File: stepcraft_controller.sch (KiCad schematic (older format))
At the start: 67 parts, among them J1 USB, J2 X1, J3 ISP, J4 Probe, J5 Spindle, J6 Serial, SW1 RST, U1 ADuM1201BR, U2 ATMEGA328P-AU, U3 CP2102, U4 ADuM1201BR, Y1 Crystal

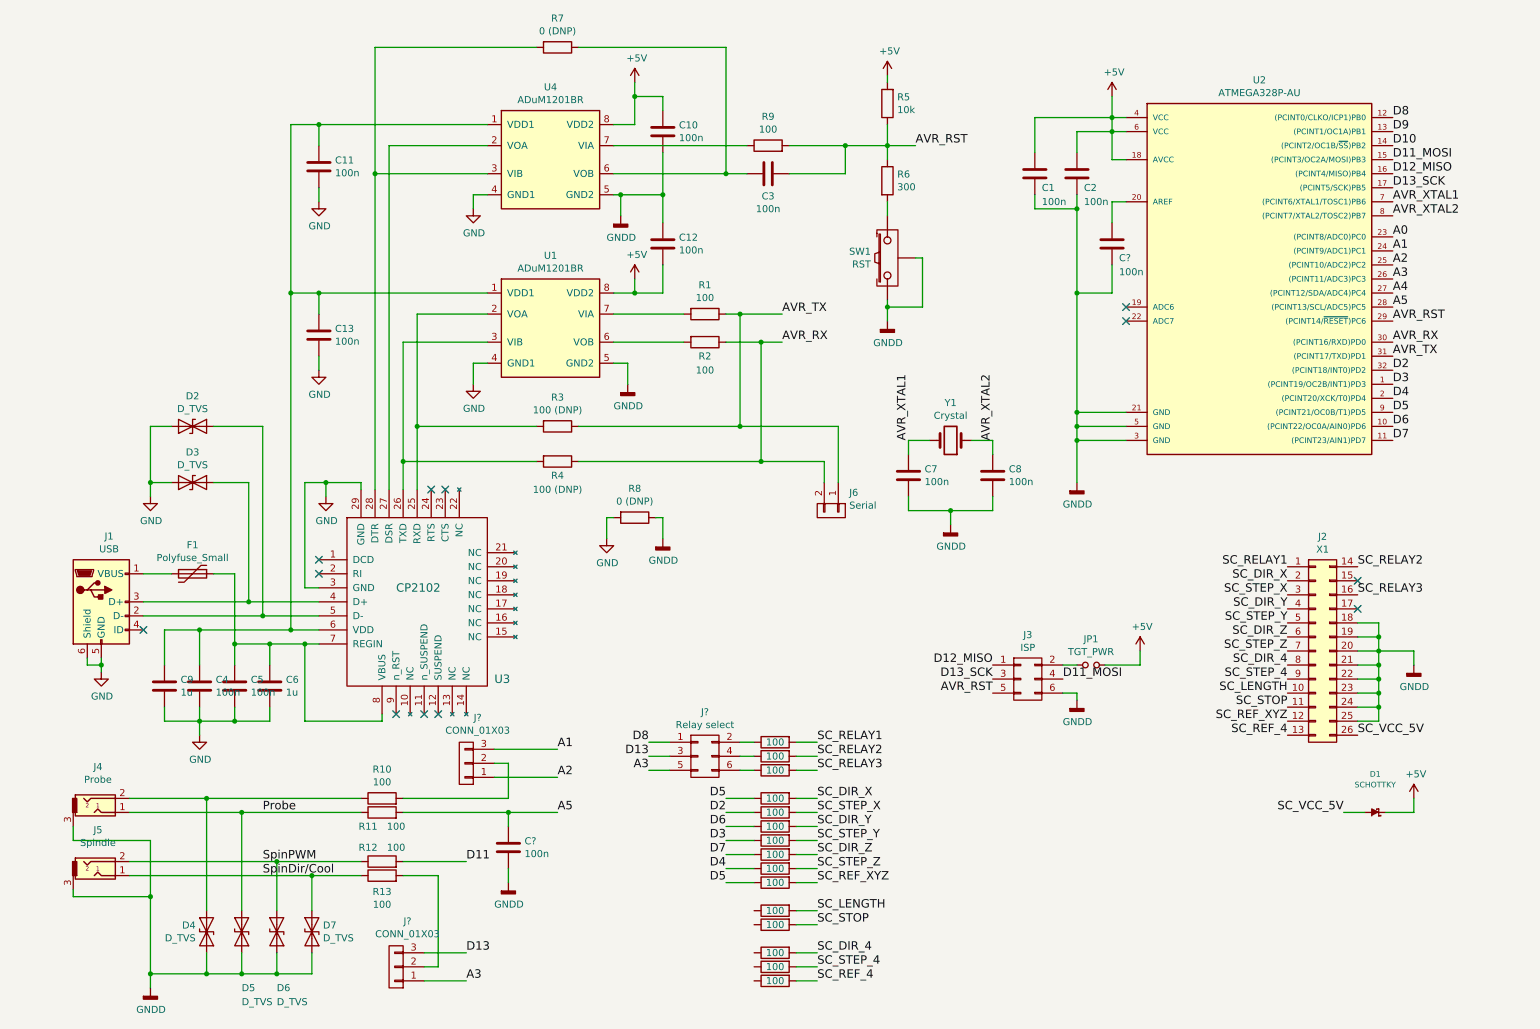
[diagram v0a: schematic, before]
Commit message: Update schematics and board, fully routed board
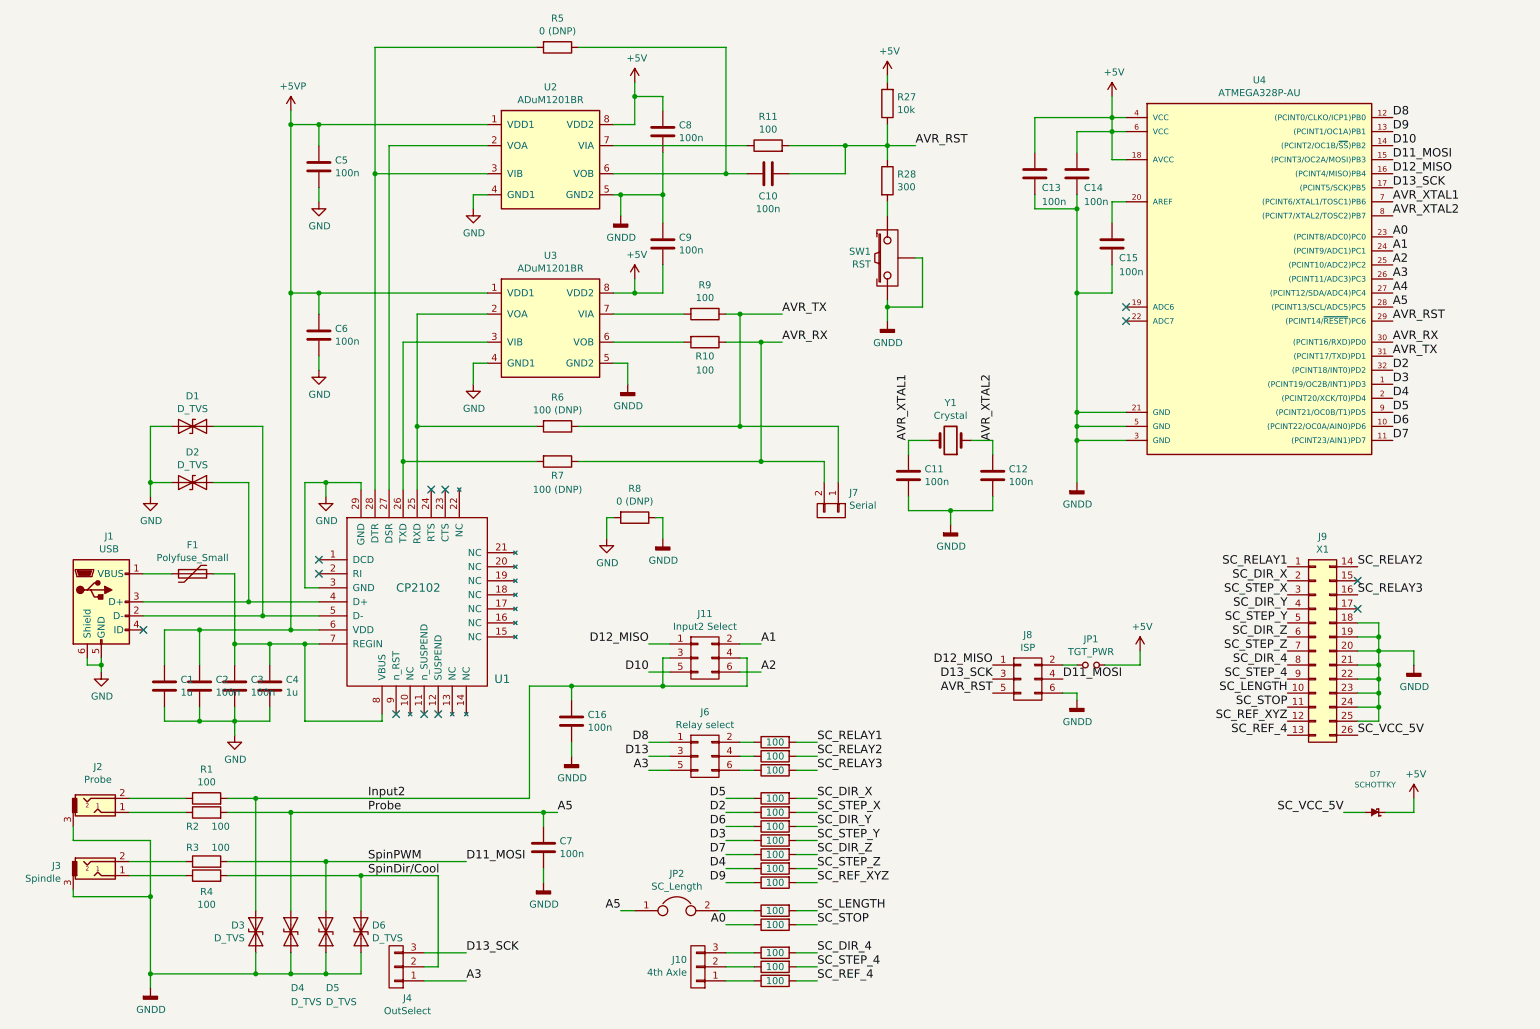
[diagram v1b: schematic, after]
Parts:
- removed J?: CONN_01X03, symbol CONN_01X03
- added C16: 100n, Capacitors_SMD:C_0805, symbol C
- added J10: 4th Axle, Pin_Headers:Pin_Header_Straight_1x03_Pitch2.54mm, symbol CONN_01X03
- added J11: Input2 Select, Pin_Headers:Pin_Header_Straight_2x03_Pitch2.54mm, symbol CONN_02X03
- added JP2: SC_Length, Pin_Headers:Pin_Header_Straight_1x02_Pitch2.54mm, symbol Jumper
- J1: footprint w_conn_pc:conn_usb_B_micro_smd -> iotta_footprints:conn_usb_B_micro_smd
- J4: renamed from J?; value CONN_01X03 -> OutSelect; footprint (none) -> Pin_Headers:Pin_Header_Straight_1x03_Pitch2.54mm
- J6: renamed from J?; footprint Pin_Headers:Pin_Header_Angled_2x03_Pitch2.54mm -> Pin_Headers:Pin_Header_Straight_2x03_Pitch2.54mm
- gave numbers to parts that had none: 17
- renumbered C9 to C1, C3 to C10, C7 to C11, C8 to C12, C1 to C13, C2 to C14, C4 to C2, C5 to C3, C6 to C4, C11 to C5, C13 to C6, C10 to C8, C12 to C9, D2 to D1, D3 to D2, D4 to D3, D5 to D4, D6 to D5, D7 to D6, D1 to D7, J4 to J2, J5 to J3, J6 to J7, J3 to J8, J2 to J9, R10 to R1, R2 to R10, R9 to R11, R11 to R2, R5 to R27, R6 to R28, R12 to R3, R13 to R4, R7 to R5, R3 to R6, R4 to R7, R1 to R9, U3 to U1, U4 to U2, U1 to U3, U2 to U4
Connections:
- net D11 is gone; now on net D11_MOSI: R3.2
- net A0: now also R23.1
- net A1: now also J11.2 (P2)
- net A2: now also J11.6 (P6)
- net A5: now also D4.1 (A1), JP2.1
- net D10: now also J11.5 (P5)
- net D11_MOSI: now also D5.1 (A1)
- net D12_MISO: now also J11.1 (P1)
- net D13: no longer J4.3 (P3)
- net D13_SCK: now also J4.3 (P3)
- net D5: no longer R21.1
- net D9: now also R21.1
- net GNDD: now also C16.2
- net SpinDir/Cool: now also J4.2 (P2), R4.2; no longer J3.1, R4.1
- net +5VP: now reaches C1.1, C2.1, C5.1, C6.1, U1.6 (VDD), U2.1 (VDD1), U3.1 (VDD1)
- net at J2.2, R1.1: no longer D3.1 (A1)
- net Input2: now reaches R1.2
- net Input2: now also D3.1 (A1), C16.1, J11.3 (P3), J11.4 (P4)
- net at R24.1: now also J10.3 (P3)
- net at R25.1: now also J10.2 (P2)
- net at R22.1: now also JP2.2
- net at R26.1: now also J10.1 (P1)
- net Probe: no longer names the net of J2.1, R2.1
- net Probe: no longer D4.1 (A1)
- net SpinPWM: no longer names the net of J3.2, R3.1
- net SpinPWM: no longer D5.1 (A1)
- new net: J3.1, R4.1
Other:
- moved on the sheet: C7, D3, D4, D5, D6, R1, R2, R3, R4

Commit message: Update PCB routing.
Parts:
- JP1: value TGT_PWR -> ISP_PWR
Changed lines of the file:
@@
 P 7900 5200
 F 0 "JP1" H 7900 5385 50  0000 C CNN
-F 1 "TGT_PWR" H 7900 5294 50  0000 C CNN
+F 1 "ISP_PWR" H 7900 5294 50  0000 C CNN
 F 2 "Pin_Headers:Pin_Header_Straight_1x02_Pitch2.54mm" H 7900 5200 50  0001 C CNN
 F 3 "" H 7900 5200 50  0001 C CNN
@@
 U 1 1 59977BF2
 P 1550 5350
-F 0 "C2" H 1665 5396 50  0000 L CNN
-F 1 "100n" H 1665 5305 50  0000 L CNN
+F 0 "C2" H 1600 5250 50  0000 L CNN
+F 1 "100n" H 1600 5150 50  0000 L CNN
 F 2 "Capacitors_SMD:C_0805" H 1588 5200 50  0001 C CNN
 F 3 "" H 1550 5350 50  0001 C CNN
@@
 U 1 1 599780B8
 P 1800 5350
-F 0 "C3" H 1915 5396 50  0000 L CNN
-F 1 "100n" H 1915 5305 50  0000 L CNN
+F 0 "C3" H 1850 5250 50  0000 L CNN
+F 1 "100n" H 1850 5150 50  0000 L CNN
 F 2 "Capacitors_SMD:C_0805" H 1838 5200 50  0001 C CNN
 F 3 "" H 1800 5350 50  0001 C CNN
@@
 U 1 1 59978104
 P 2050 5350
-F 0 "C4" H 2165 5396 50  0000 L CNN
-F 1 "1u" H 2165 5305 50  0000 L CNN
+F 0 "C4" H 2100 5250 50  0000 L CNN
+F 1 "1u" H 2100 5150 50  0000 L CNN
 F 2 "Capacitors_SMD:C_0805" H 2088 5200 50  0001 C CNN
 F 3 "" H 2050 5350 50  0001 C CNN
@@
 U 1 1 59979C28
 P 1300 5350
-F 0 "C1" H 1415 5396 50  0000 L CNN
-F 1 "1u" H 1415 5305 50  0000 L CNN
+F 0 "C1" H 1350 5250 50  0000 L CNN
+F 1 "1u" H 1350 5150 50  0000 L CNN
 F 2 "Capacitors_SMD:C_0805" H 1338 5200 50  0001 C CNN
 F 3 "" H 1300 5350 50  0001 C CNN

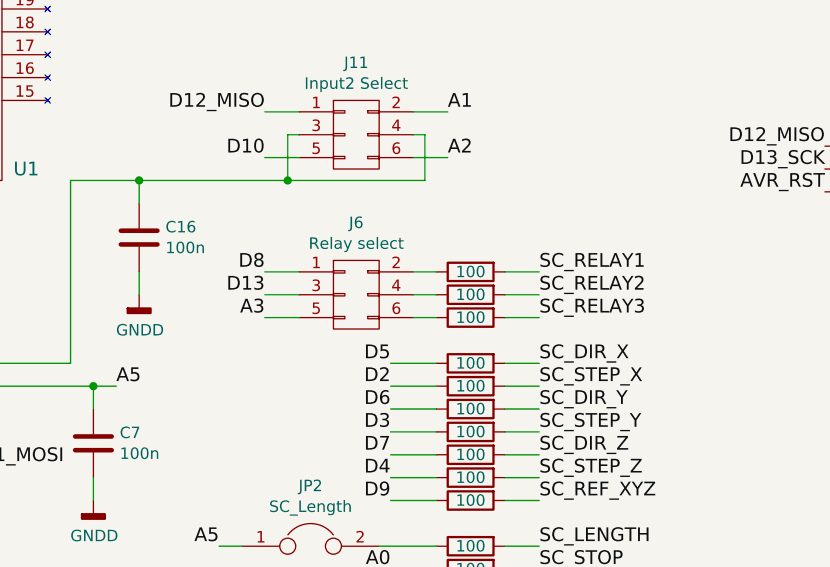
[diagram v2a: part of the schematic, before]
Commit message: Fix net name (D13), improved routing, ground plane continuity.
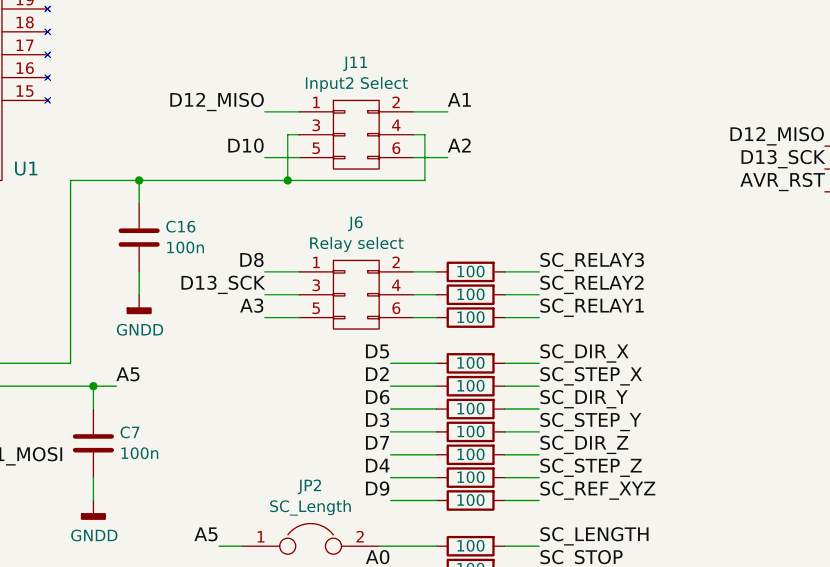
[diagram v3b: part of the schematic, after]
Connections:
- net D13 is gone; now on net D13_SCK: J6.3 (P3)
- net at R12.1: now also J6.6 (P6); no longer J6.2 (P2)
- net at R14.1: now also J6.2 (P2); no longer J6.6 (P6)
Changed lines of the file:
@@
 	1    0    0    -1
 $EndComp
-Text Label 5950 5750 0    60   ~ 0
+Text Label 5950 5950 0    60   ~ 0
 SC_RELAY1
 Text Label 5950 6150 0    60   ~ 0
@@
 L R R12
 U 1 1 59B35B24
-P 5650 5750
-F 0 "R12" V 5750 5750 50  0001 C CNN
-F 1 "100" V 5650 5750 50  0000 C CNN
-F 2 "Resistors_SMD:R_0805" V 5580 5750 50  0001 C CNN
-F 3 "" H 5650 5750 50  0001 C CNN
-	1    5650 5750
+P 5650 5950
+F 0 "R12" V 5750 5950 50  0001 C CNN
+F 1 "100" V 5650 5950 50  0000 C CNN
+F 2 "Resistors_SMD:R_0805" V 5580 5950 50  0001 C CNN
+F 3 "" H 5650 5950 50  0001 C CNN
+	1    5650 5950
 	0    -1   1    0
 $EndComp
@@
 	0    -1   1    0
 $EndComp
-Text Label 5950 5950 0    60   ~ 0
+Text Label 5950 5750 0    60   ~ 0
 SC_RELAY3
 Text Label 5950 5850 0    60   ~ 0
@@
 L R R14
 U 1 1 59B37BAF
-P 5650 5950
-F 0 "R14" V 5750 5950 50  0001 C CNN
-F 1 "100" V 5650 5950 50  0000 C CNN
-F 2 "Resistors_SMD:R_0805" V 5580 5950 50  0001 C CNN
-F 3 "" H 5650 5950 50  0001 C CNN
-	1    5650 5950
+P 5650 5750
+F 0 "R14" V 5750 5750 50  0001 C CNN
+F 1 "100" V 5650 5750 50  0000 C CNN
+F 2 "Resistors_SMD:R_0805" V 5580 5750 50  0001 C CNN
+F 3 "" H 5650 5750 50  0001 C CNN
+	1    5650 5750
 	0    -1   1    0
 $EndComp
@@
 Text Label 4750 5950 2    60   ~ 0
 A3
-Text Label 4750 5850 2    60   ~ 0
-D13
 Text Label 4750 5750 2    60   ~ 0
 D8
@@
 $EndComp
 Connection ~ 2200 1350
+Text Label 4750 5850 2    60   ~ 0
+D13_SCK
 $EndSCHEMATC

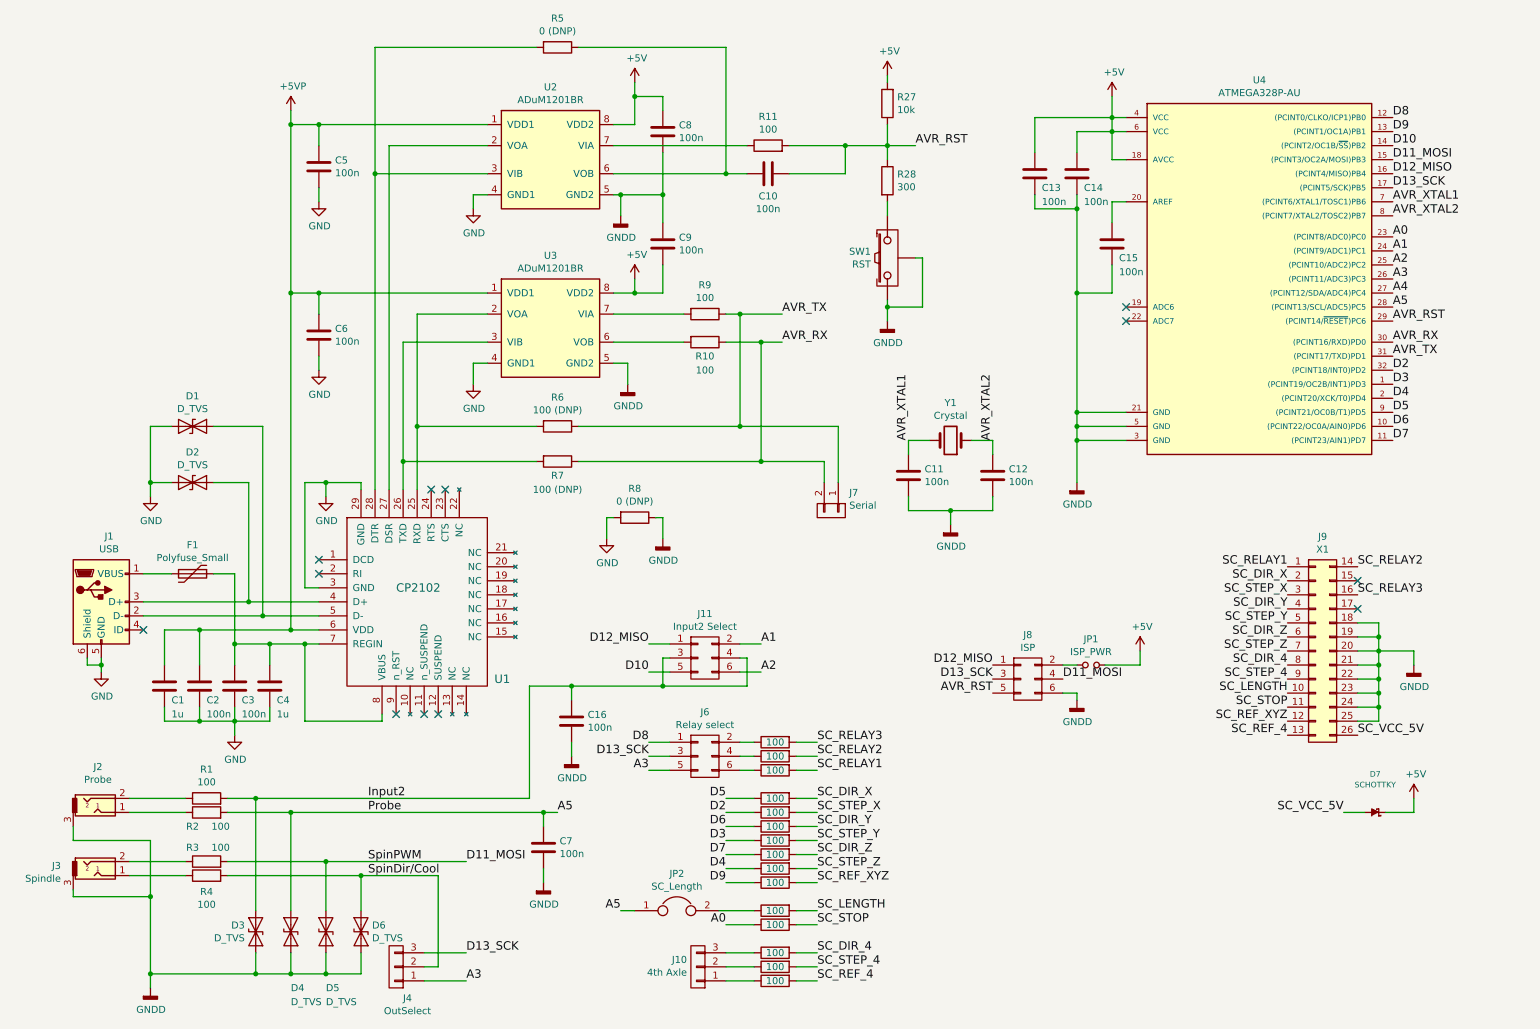
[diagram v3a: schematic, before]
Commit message: Change SiLabs CP2102 QFN-28 to (more common) CP2102N QFN-24
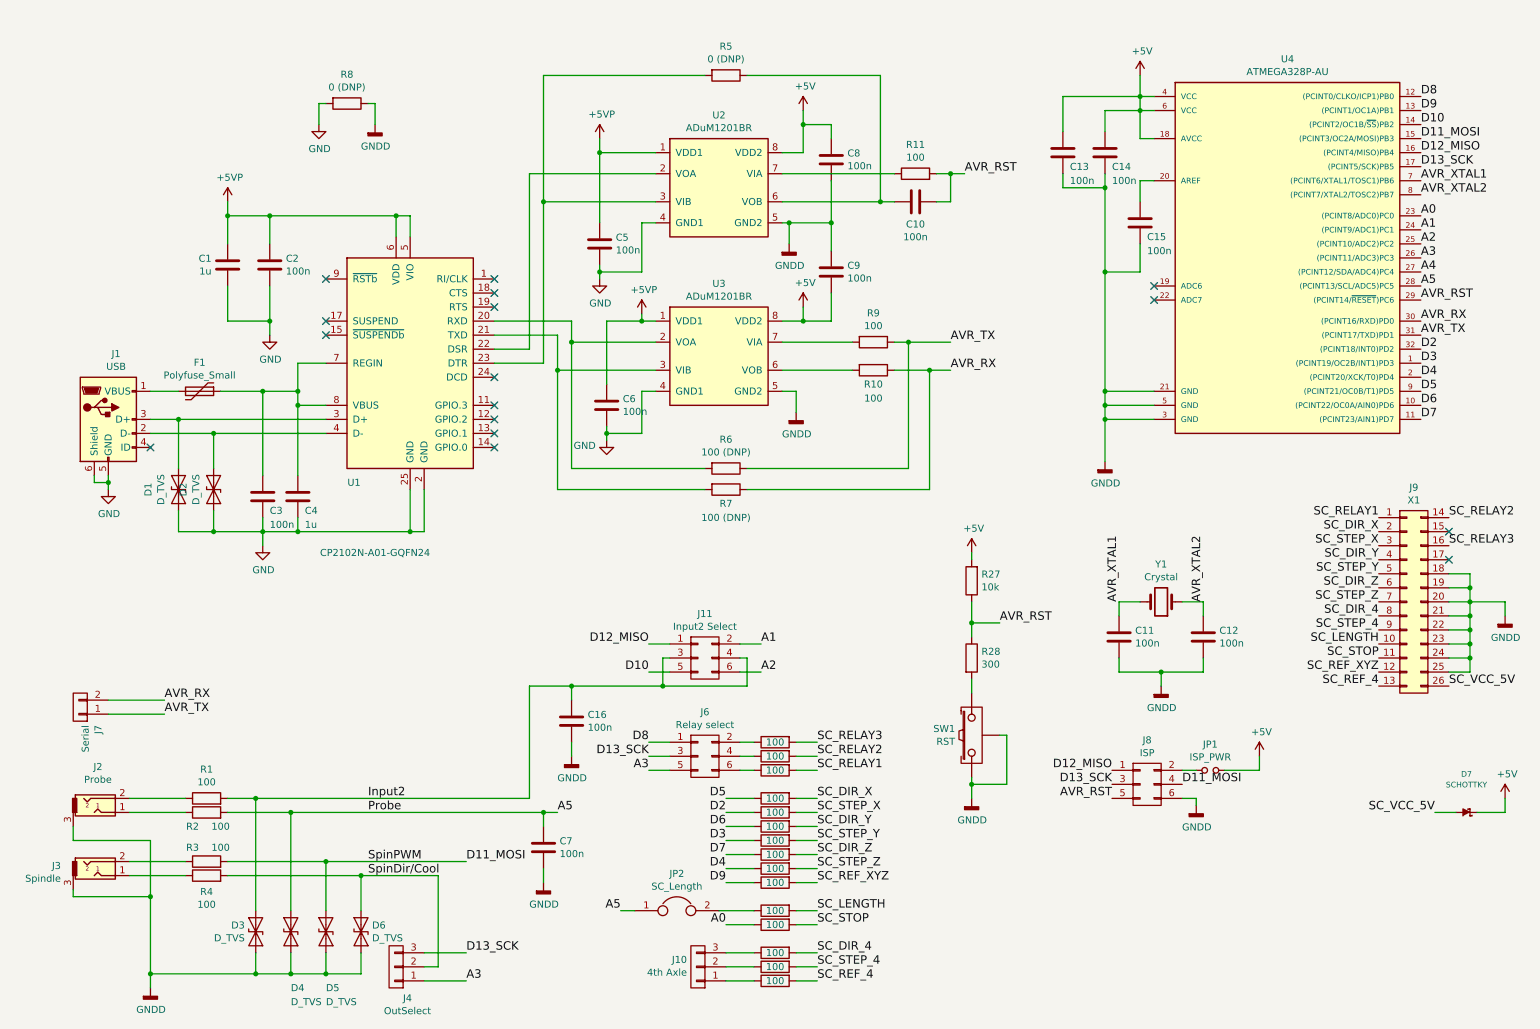
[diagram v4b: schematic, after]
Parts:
- removed U1: CP2102, Housings_DFN_QFN:QFN-28-1EP_5x5mm_Pitch0.5mm, symbol CP2102
- added U1: CP2102N-A01-GQFN24, Housings_DFN_QFN:QFN-24-1EP_4x4mm_Pitch0.5mm, symbol CP2102N-A01-GQFN24
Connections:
- net +5VP: now also U1.5 (VIO), U1.6 (VDD)
- net GND: now also U1.2 (GND), U1.25 (GND)
- net at R6.2, U3.2 (VOA): now also U1.20 (RXD)
- net at R7.2, U3.3 (VIB): now also U1.21 (TXD)
- net at C3.1, C4.1, F1.1: now also U1.7 (REGIN), U1.8 (VBUS)
- net at J1.2 (D-): now also D2.2 (A2), U1.4 (D-); no longer D1.2 (A2)
- net at J1.3 (D+): now also D1.2 (A2), U1.3 (D+); no longer D2.2 (A2)
- net at U2.2 (VOA): now also U1.22 (DSR)
- net at R5.2, U2.3 (VIB): now also U1.23 (DTR)
- no-connect marks 12 -> 16
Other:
- moved on the sheet: C1, C10, C11, C12, C13, C14, C15, C2, C3, C4, C5, C6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
